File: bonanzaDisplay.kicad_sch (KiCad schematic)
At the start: 30 parts, among them J15 BM03B-SRSS-TB, J2 USB_C_Receptacle_USB2.0, J5 Conn_01x10, SW1 TS-1088-AR02016, SW2 TS-1088-AR02016, U1 RP2354A, Y1 ABM8-272-T3

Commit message: add display connector and circuit
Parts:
- added C19, C35: 0.1uF, Capacitor_SMD:C_0402_1005Metric, symbol Device:C_Small
- added C21, C26: 4.7uF, Capacitor_SMD:C_0402_1005Metric, symbol Device:C_Small
- added C22: 1uF, Capacitor_SMD:C_0402_1005Metric, symbol Device:C_Small
- added C29: 3.3nF, Capacitor_SMD:C_0402_1005Metric, symbol Device:C_Small
- added C34: 22uF, Capacitor_SMD:C_1206_3216Metric, symbol Device:C_Small
- added C36: 10uF, Capacitor_SMD:C_0402_1005Metric, symbol Device:C_Small
- added C8: 10uF, Capacitor_SMD:C_0603_1608Metric, symbol Device:C_Small
- added D1, D2: 1N4148, Diode_THT:D_DO-35_SOD27_P7.62mm_Horizontal, symbol Device:D_Filled
- added J1: OLED-1.31-SSD1322, symbol bonanzaDisplay:OLED-3.12-SSD1322
- added R12: 309k, Resistor_SMD:R_0402_1005Metric, symbol Device:R_Small_US
- added R13: 100k, Resistor_SMD:R_0402_1005Metric, symbol Device:R_Small_US
- added R34: 50, Resistor_SMD:R_0402_1005Metric, symbol Device:R_Small_US
- added R35: 910k, Resistor_SMD:R_0402_1005Metric, symbol Device:R_Small_US
- added TP9: 3V3, bitaxe:TestPoint_Pad_D1.0mm, symbol Connector:TestPoint
- added U10: TPS82130, bitaxe:Texas_SIL0008D_MicroSiP-8-1EP_2.8x3mm_P0.65mm_EP1.1x1.9mm_ThermalVias, symbol bonanzaDisplay:TPS82130
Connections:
- net 12V: now also C35.1, C36.1, C8.2, J1.29 (VCC), J1.3 (VCC), U10.1 (EN), U10.2 (VIN)
- net 3V3: now also C19.1, C21.1, C34.2, J1.17 (BS1), J1.24 (VDDIO), J1.26 (VCI), R12.2, TP9.1, U10.4 (VOUT), U10.5 (VOUT)
- net GND: now also C19.2, C21.2, C22.2, C26.2, C29.1, C34.1, C35.2, C36.2, C8.1, D2.1 (K), J1.1 (NC_(GND)), J1.16 (BS0), J1.2 (VSS), J1.28 (VLSS), J1.30 (NC_(GND)), J1.5 (VLSS), R13.1, R35.2, U10.3 (GND), U10.9 (GND)
- net D7: now reaches U1.10 (GPIO7)
- net D7: now also J1.6 (D7)
- net E/RD: now reaches U1.12 (GPIO8)
- net E/RD: now also J1.14 (E/RD)
- net R/W: now reaches U1.13 (GPIO9)
- net R/W: now also J1.15 (R/W)
- net DC: now reaches U1.14 (GPIO10)
- net DC: now also J1.18 (DC)
- net RES: now reaches U1.15 (GPIO11)
- net RES: now also J1.20 (RES)
- net CS: now reaches U1.16 (GPIO12)
- net CS: now also J1.19 (CS)
- net D0: now reaches U1.2 (GPIO0)
- net D0: now also J1.13 (D0)
- net D1: now reaches U1.3 (GPIO1)
- net D1: now also J1.12 (D1)
- net D2: now reaches U1.4 (GPIO2)
- net D2: now also J1.11 (D2)
- net D3: now reaches U1.5 (GPIO3)
- net D3: now also J1.10 (D3)
- net D4: now reaches U1.7 (GPIO4)
- net D4: now also J1.9 (D4)
- net D5: now reaches U1.8 (GPIO5)
- net D5: now also J1.8 (D5)
- net D6: now reaches U1.9 (GPIO6)
- net D6: now also J1.7 (D6)
- new net: C26.1, J1.4 (VCOMH)
- new net: R12.1, R13.2, U10.6 (FB)
- new net: C29.2, U10.8 (SS/TR)
- new net: D1.1 (K), D2.2 (A)
- new net: D1.2 (A), R34.1
- new net: J1.27 (VSL), R34.2
- new net: J1.22 (IREF), R35.1
- new net: C22.1, J1.25 (VDD)
- no-connect marks 4 -> 7
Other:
- moved on the sheet: C14, C15, C16, C17, C18, C20, C23, C24, C25, C27, C28, C30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

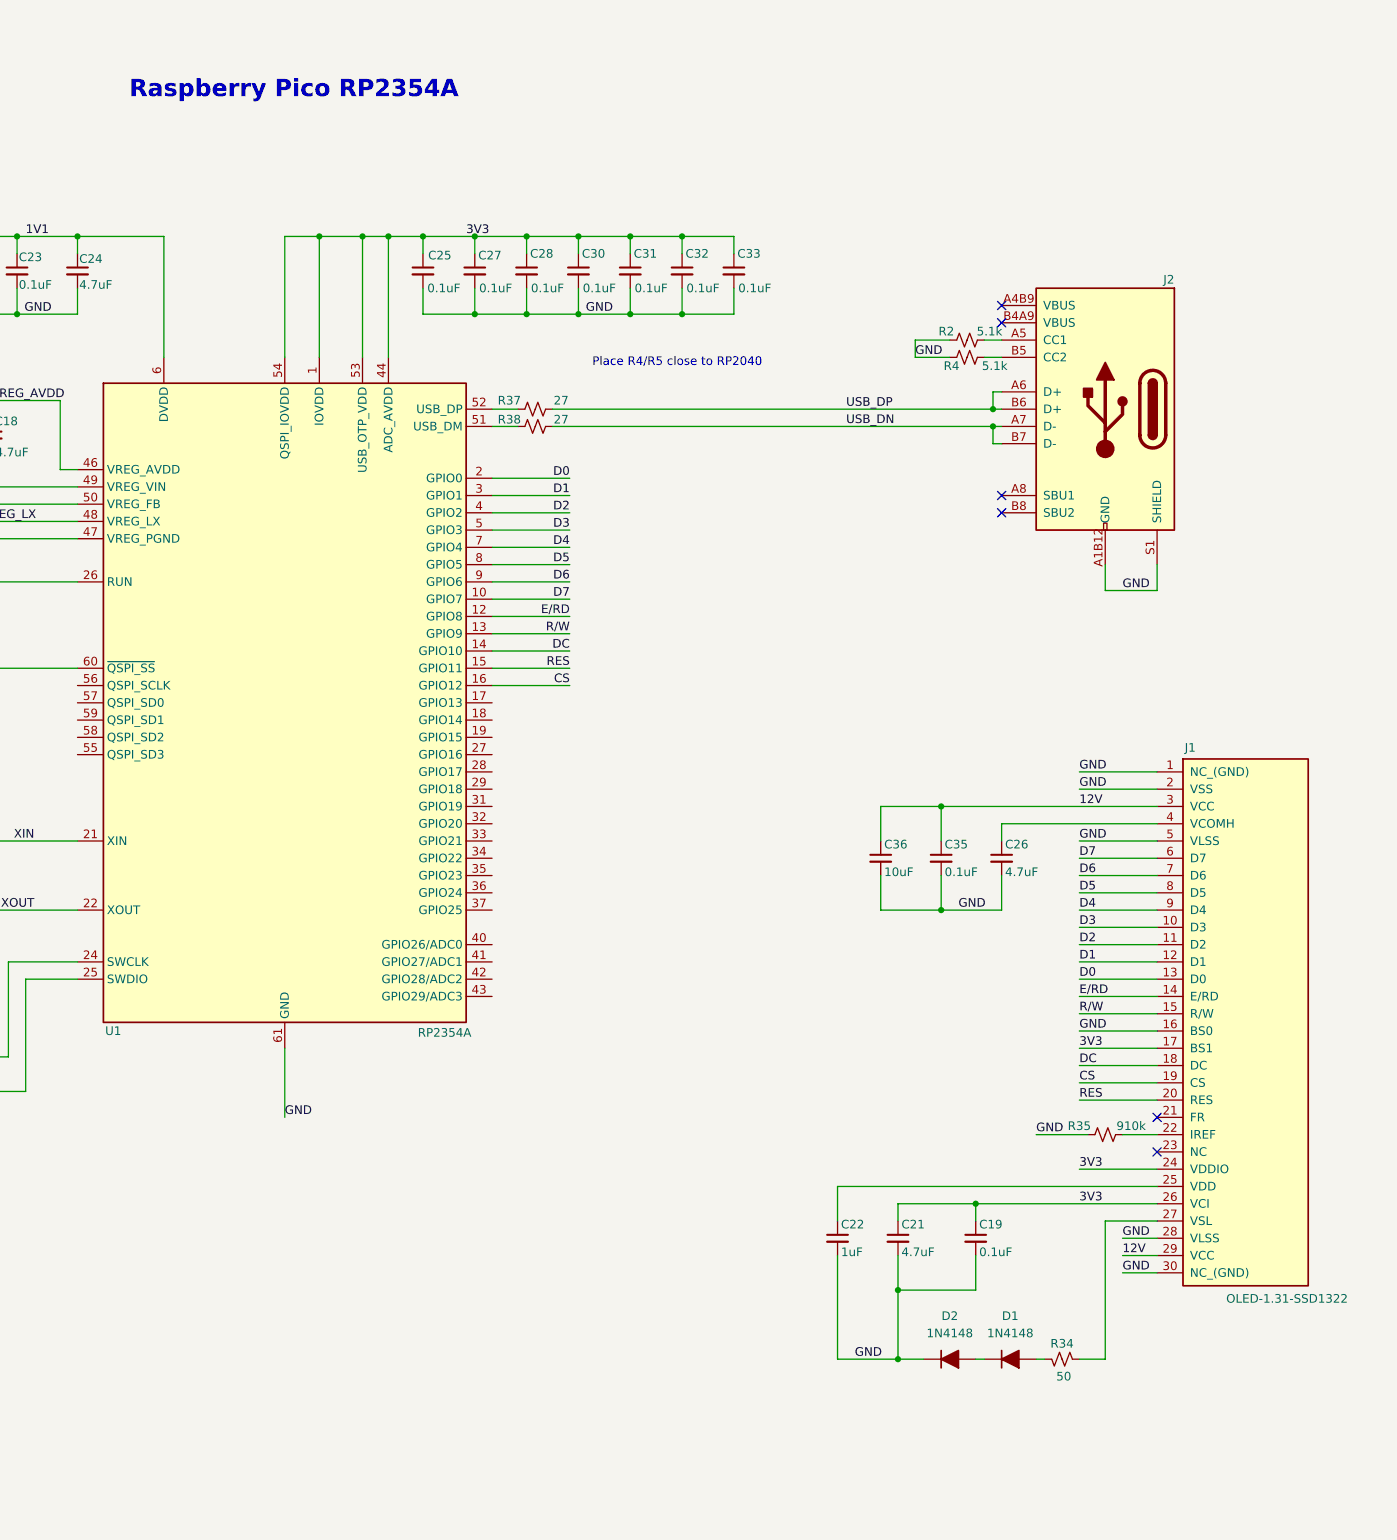
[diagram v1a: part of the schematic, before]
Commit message: updated display circuit with reference design
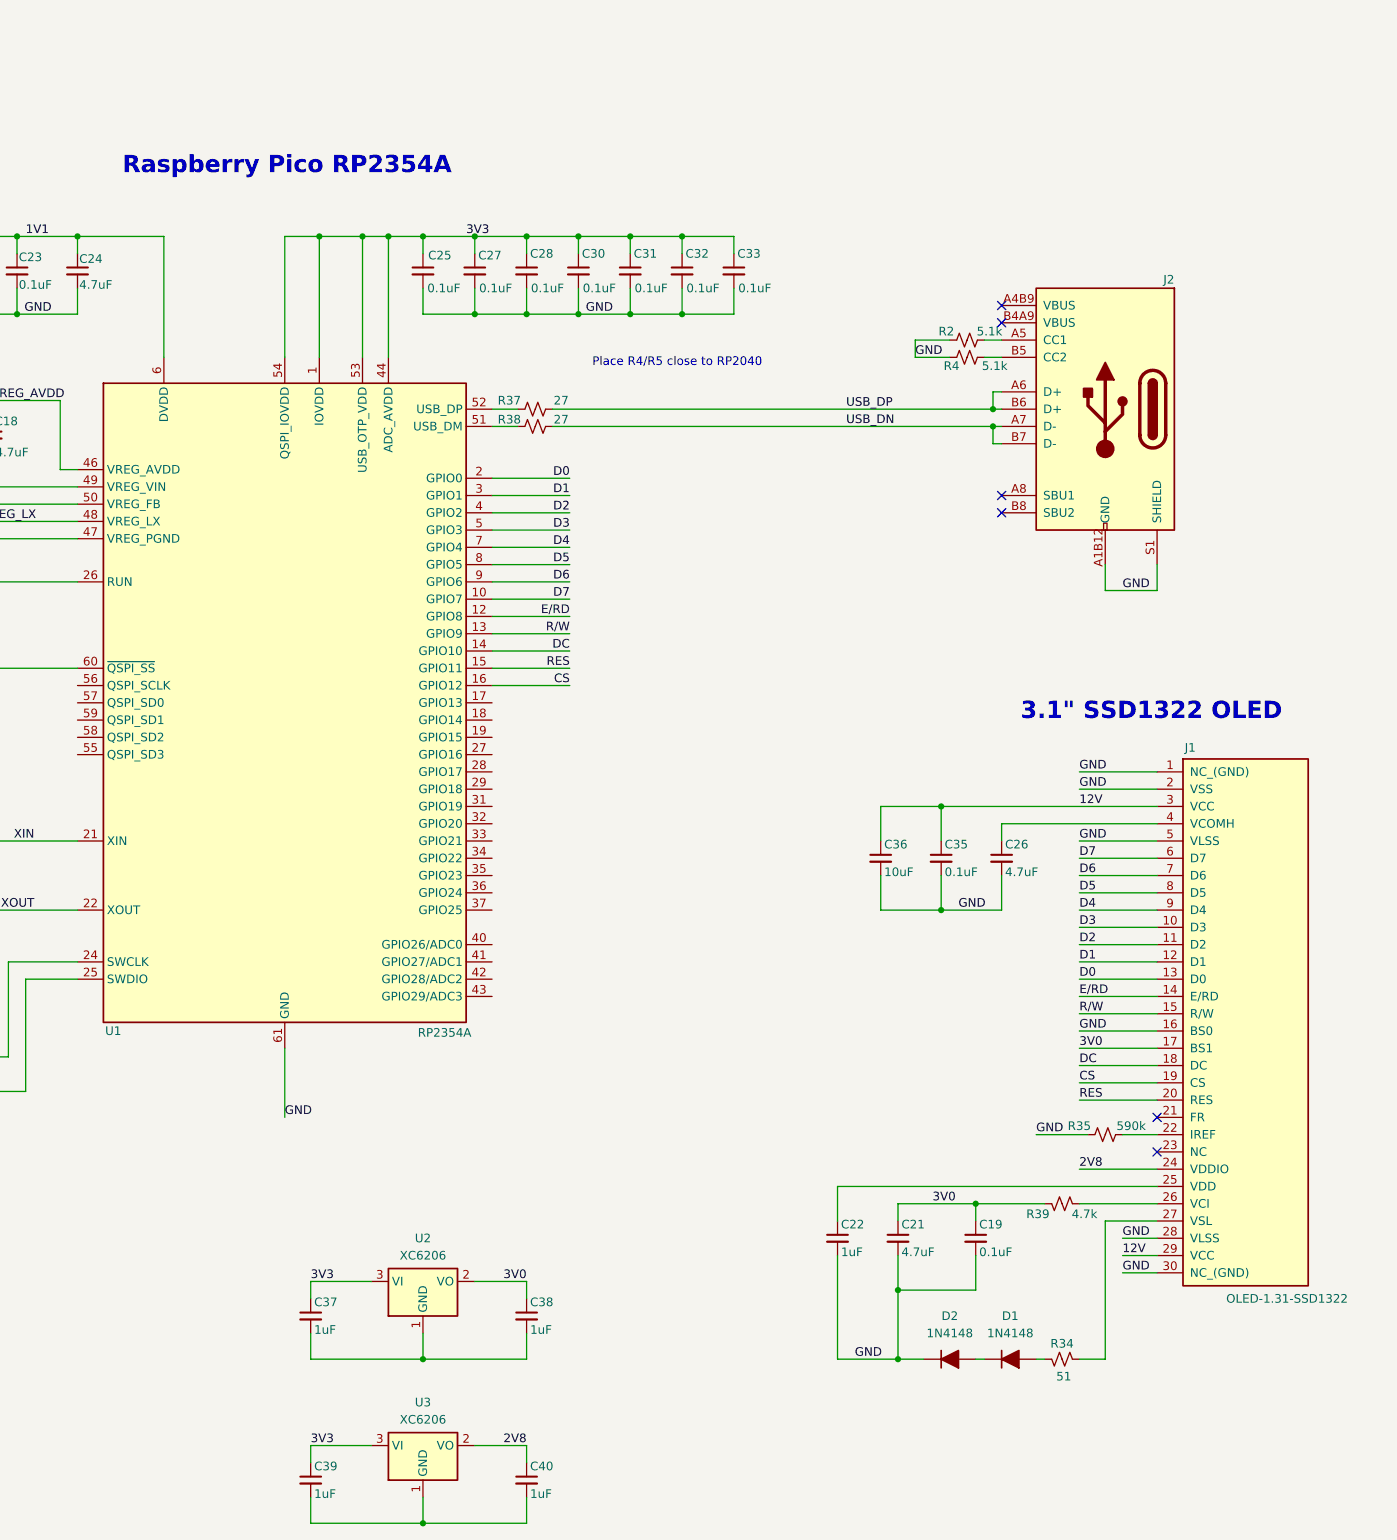
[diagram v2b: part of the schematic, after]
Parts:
- added C37, C38, C39, C40: 1uF, Capacitor_SMD:C_0402_1005Metric, symbol Device:C_Small
- added R39: 4.7k, Resistor_SMD:R_0402_1005Metric, symbol Device:R_Small_US
- added U2, U3: XC6206, Package_TO_SOT_SMD:SOT-23, symbol bonanzaDisplay:XC6206
- R34: value 50 -> 51
- R35: value 910k -> 590k
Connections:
- net 3V3: now also C37.1, C39.1, U2.3 (VI), U3.3 (VI); no longer C19.1, C21.1, J1.17 (BS1), J1.24 (VDDIO), J1.26 (VCI)
- new net: J1.26 (VCI), R39.2
- new net: C37.2, C38.2, U2.1 (GND)
- new net: C39.2, C40.2, U3.1 (GND)
- new net 2V8: C40.1, J1.24 (VDDIO), U3.2 (VO)
- new net 3V0: C19.1, C21.1, C38.1, J1.17 (BS1), R39.1, U2.2 (VO)
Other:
- note added: "3.1" SSD1322 OLED"

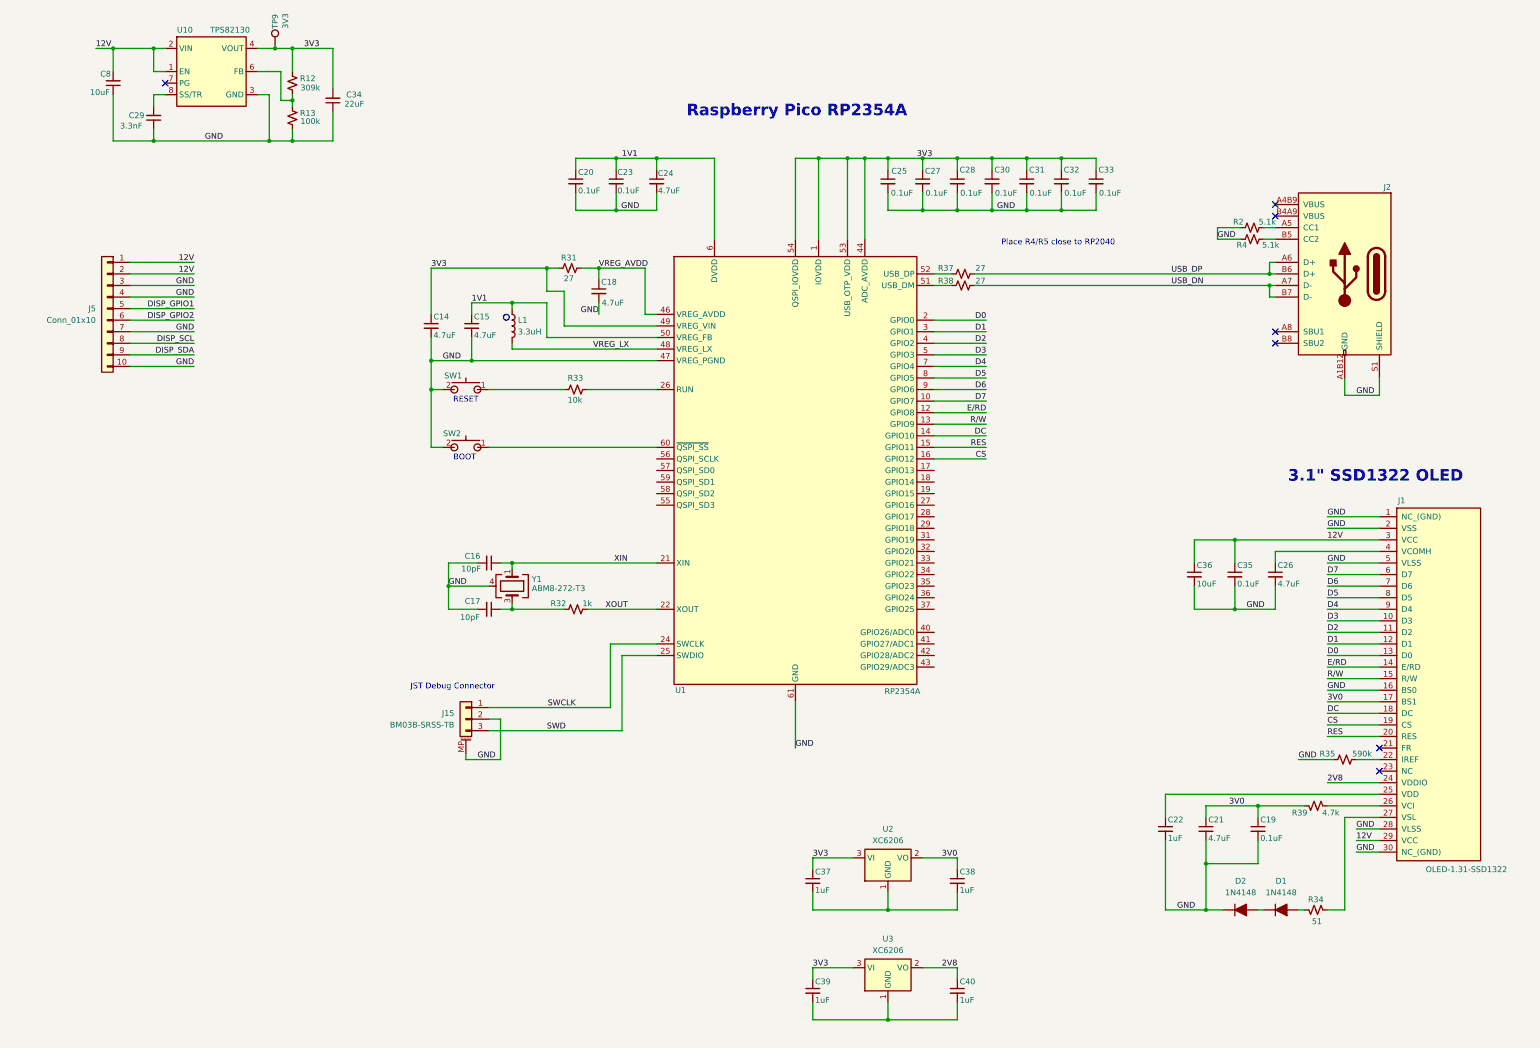
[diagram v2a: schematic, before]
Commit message: added nav switch. added part footprints to local library
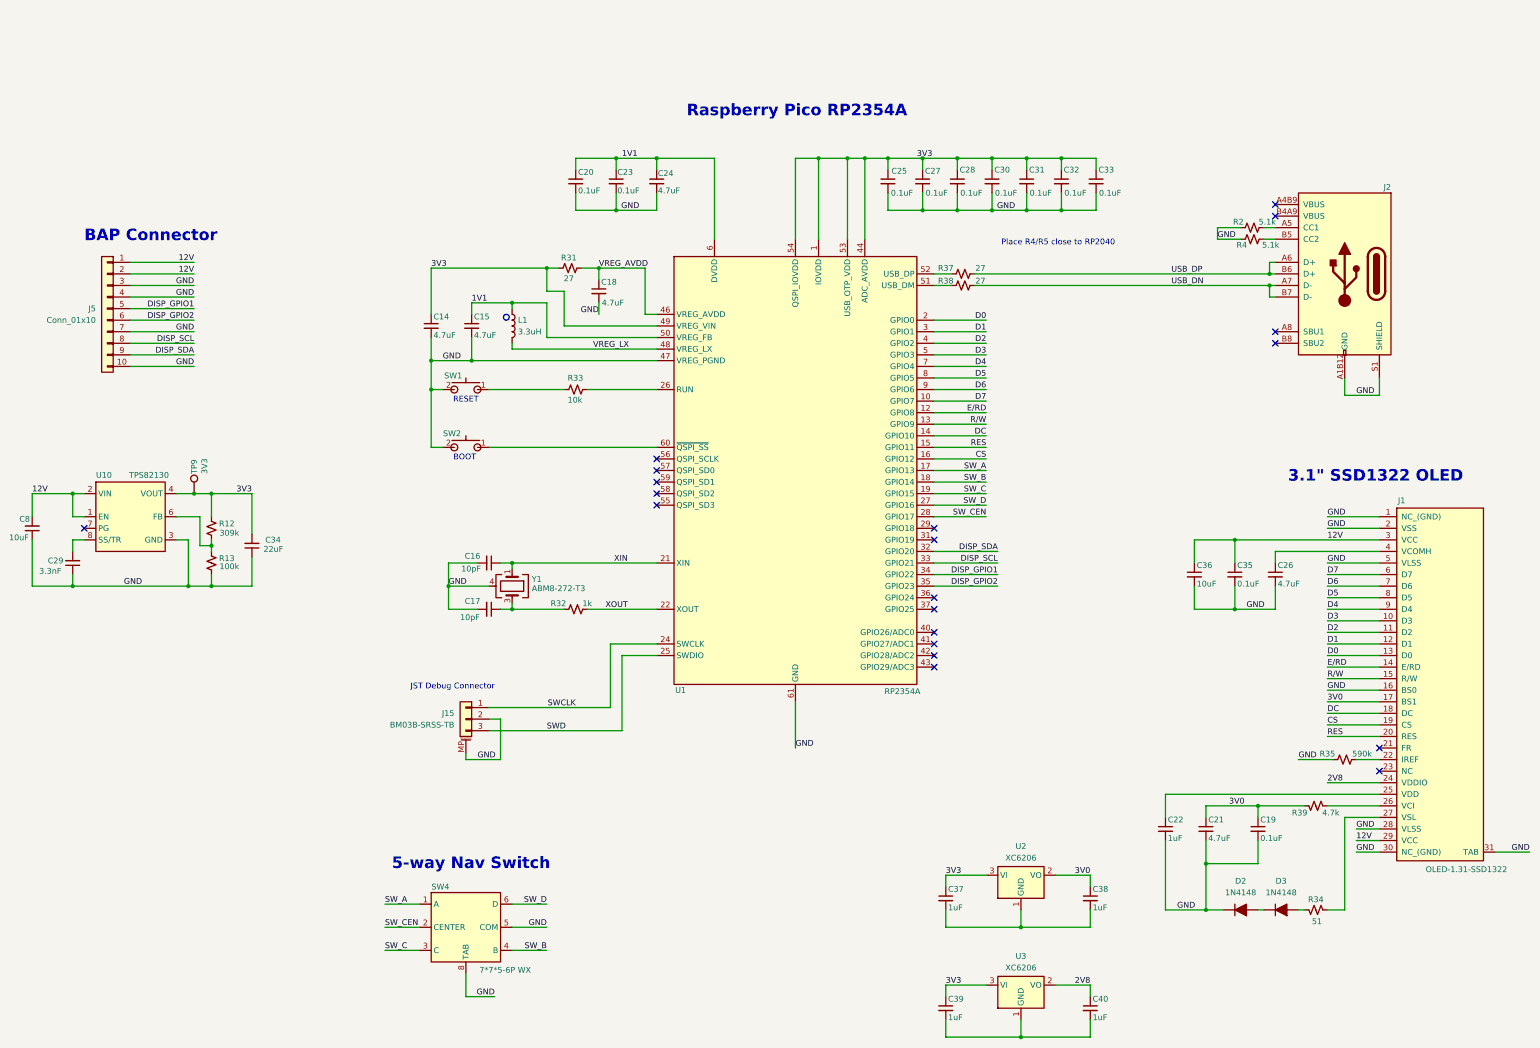
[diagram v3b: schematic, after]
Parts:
- removed D1: 1N4148, Diode_THT:D_DO-35_SOD27_P7.62mm_Horizontal, symbol Device:D_Filled
- added D3: 1N4148, Diode_SMD:D_SOD-523, symbol Device:D_Filled
- added SW4: 7*7*5-6P WX, bonanzaDisplay:SW-SMD_6P-L7.0-W7.0-P1.40-LS7.4-TL, symbol bonanzaDisplay:tactile-switch-5way
- C36: footprint Capacitor_SMD:C_0402_1005Metric -> Capacitor_SMD:C_0805_2012Metric
- D2: footprint Diode_THT:D_DO-35_SOD27_P7.62mm_Horizontal -> Diode_SMD:D_SOD-523; DK (none) -> 1N4148WTCT-ND; PARTNO (none) -> 1N4148WT
- J1: footprint (none) -> bonanzaDisplay:FPC-SMD_P0.50-30P_LCS-SJ-H2.0
- J2: footprint bitcrane:USB_C_Receptacle_GCT_USB4105-xx-A_16P_TopMnt_Horizontal -> bitaxeBonanza:USB_C_Receptacle_GCT_USB4105-xx-A_16P_TopMnt_Horizontal
- J5: footprint bitaxe:CONN10_1-1735042-0 -> bonanzaDisplay:CONN10_1-1735042-0
- U10: footprint bitaxe:Texas_SIL0008D_MicroSiP-8-1EP_2.8x3mm_P0.65mm_EP1.1x1.9mm_ThermalVias -> bonanzaDisplay:Texas_SIL0008D_MicroSiP-8-1EP_2.8x3mm_P0.65mm_EP1.1x1.9mm_ThermalVias
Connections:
- net DISP_GPIO1: now also U1.34 (GPIO22)
- net DISP_GPIO2: now also U1.35 (GPIO23)
- net DISP_SCL: now also U1.33 (GPIO21)
- net DISP_SDA: now also U1.32 (GPIO20)
- net GND: now also J1.31 (TAB), J1.32 (TAB), SW4.5 (COM), SW4.7 (TAB), SW4.8 (TAB)
- net at D2.2 (A): now also D3.1 (K)
- net at R34.1: now also D3.2 (A)
- net SW_A: now reaches U1.17 (GPIO13)
- net SW_A: now also SW4.1 (A)
- net SW_B: now reaches U1.18 (GPIO14)
- net SW_B: now also SW4.4 (B)
- net SW_C: now reaches U1.19 (GPIO15)
- net SW_C: now also SW4.3 (C)
- net SW_D: now reaches U1.27 (GPIO16)
- net SW_D: now also SW4.6 (D)
- net SW_CEN: now reaches U1.28 (GPIO17)
- net SW_CEN: now also SW4.2 (CENTER)
- no-connect marks 7 -> 20
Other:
- note added: "5-way Nav Switch"
- note added: "BAP Connector"
- moved on the sheet: C29, C34, C37, C38, C39, C40, C8, R12, R13, TP9, U10, U2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

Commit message: added more local footprints. brought over edge cuts from bitaxeBonanza. Placed display
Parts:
- removed J2: USB_C_Receptacle_USB2.0, bitaxeBonanza:USB_C_Receptacle_GCT_USB4105-xx-A_16P_TopMnt_Horizontal, symbol bonanzaDisplay:USB_C_Receptacle_USB2.0
- added FID1, FID2, FID3, FID4: Fiducial, bonanzaDisplay:Fiducial_1mm_Mask2mm, symbol Mechanical:Fiducial
- added H1, H2, H3, H4: MountingHole_Pad, MountingHole:MountingHole_3.2mm_M3_Pad_Via, symbol Mechanical:MountingHole_Pad
- added J6: USB_C_Receptacle_USB2.0, bonanzaDisplay:USB_C_Receptacle_GCT_USB4105-xx-A, symbol bonanzaDisplay:USB_C_Receptacle_USB2.0
- J15: value BM03B-SRSS-TB -> SWD; footprint Connector_JST:JST_SH_BM03B-SRSS-TB_1x03-1MP_P1.00mm_Vertical -> Connector_PinHeader_2.54mm:PinHeader_1x03_P2.54mm_Vertical; symbol Connector_Generic_MountingPin:Conn_01x03_MountingPin -> Connector_Generic:Conn_01x03; MPN BM03B-SRSS-TB -> (none); Manufacturer JST Sales America Inc. -> (none)
- L1: footprint RP2350_60QFN_minimal:L_pol_2016 -> bonanzaDisplay:IND-SMD-L2.0-W1.6-MLP2016H3R3MT0S1; LCSC (none) -> C383379
- SW1, SW2: footprint bitcrane:SW-SMD_L3.9-W3.0-P4.45 -> bonanzaDisplay:SW-SMD_L3.9-W3.0-P4.45
- TP9: footprint bitaxe:TestPoint_Pad_D1.0mm -> bonanzaDisplay:TestPoint_Pad_D1.0mm
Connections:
- net GND: now also H1.1, H2.1, H3.1, H4.1, J6.A1 (GND), J6.B1 (GND), J6.S1 (SHIELD); no longer J15.MP (MountPin)
- net USB_DN: now also J6.A7 (D-), J6.B7 (D-)
- net USB_DP: now also J6.A6 (D+), J6.B6 (D+)
- net at R4.2: now also J6.B5 (CC2)
- net at R2.2: now also J6.A5 (CC1)
- new net: J6.A4 (VBUS), J6.B4 (VBUS)
- no-connect marks 20 -> 19
